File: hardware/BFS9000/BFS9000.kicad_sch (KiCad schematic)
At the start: 0 parts

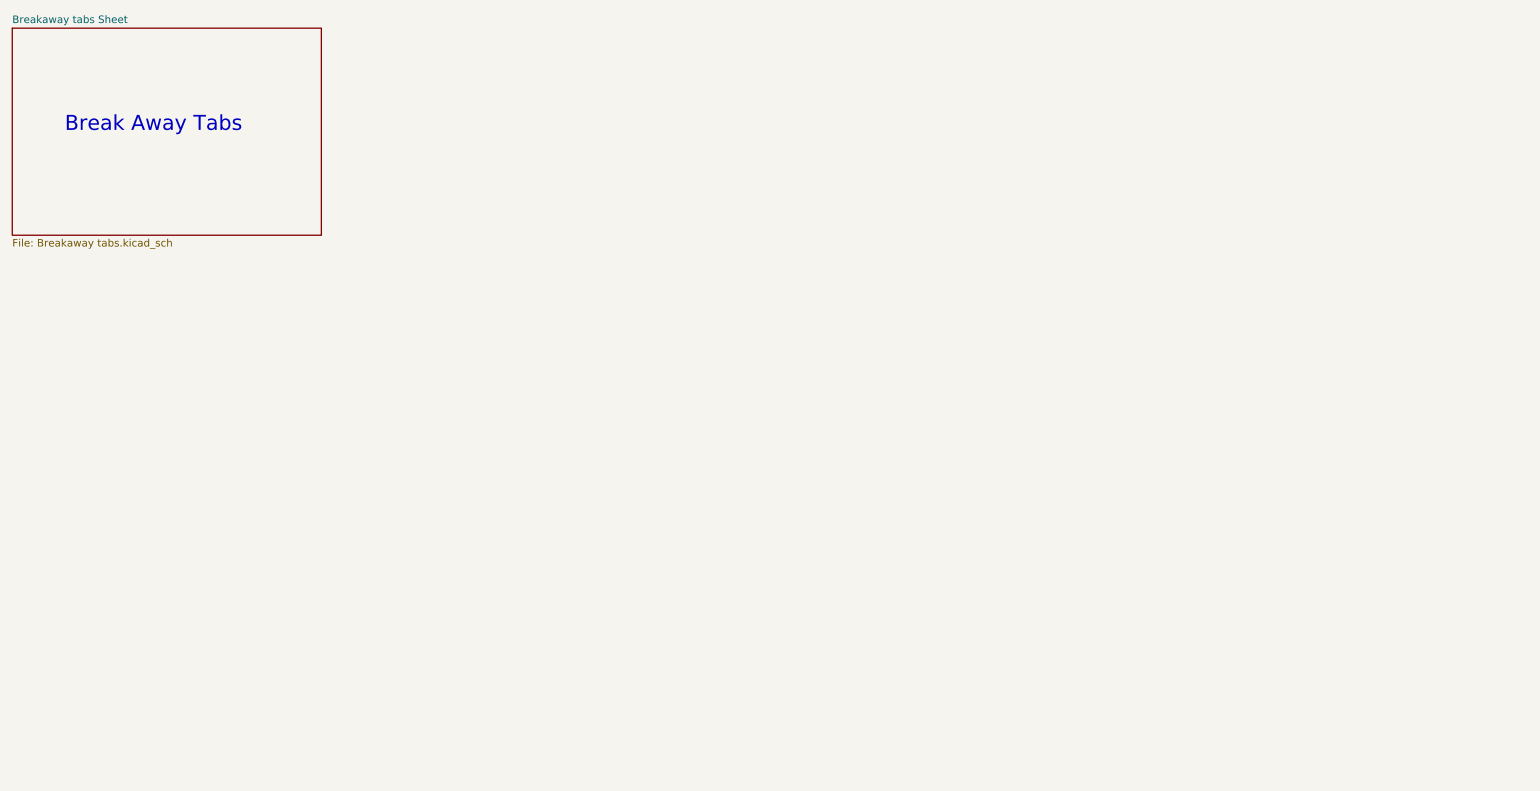
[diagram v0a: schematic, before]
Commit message: feat(hardware): add RP2040 footprint and peripheral circuitry
Add the RP2040 footprint, decoupling capacitors, OLED connectors, I2C pull-up resistors, and left/right keyboard side detection circuitry.
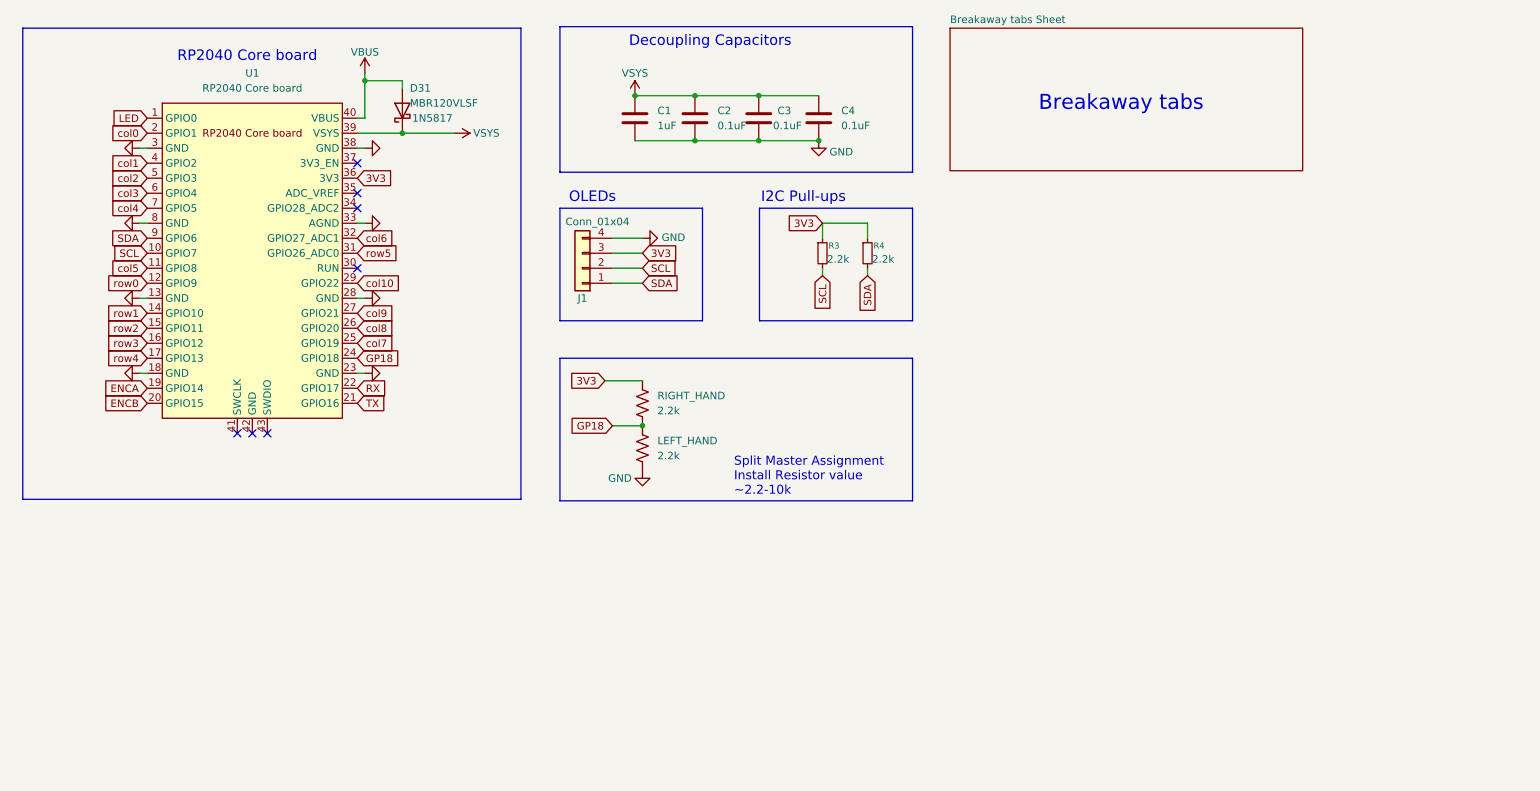
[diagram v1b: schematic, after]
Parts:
- added C1: 1uF, Capacitor_SMD:C_0805_2012Metric_Pad1.18x1.45mm_HandSolder, symbol Device:C
- added C2, C3, C4: 0.1uF, Capacitor_SMD:C_0805_2012Metric_Pad1.18x1.45mm_HandSolder, symbol Device:C
- added D31: MBR120VLSF, Sofle_Pico:D_SOD-123_DO-41_7.62mm_Hybrid_DoubleSided, symbol Diode:1N5817
- added J1: Conn_01x04, BFS9000:OLED SSD1306 128x64, symbol Connector_Generic:Conn_01x04
- added LEFT_HAND, RIGHT_HAND: 2.2k, BFS9000:Res_1206_SMD_6.3mm_TH_Hybrid, symbol Device:R_US
- added R3, R4: 2.2k, BFS9000:Res_1206_SMD_6.3mm_TH_Hybrid, symbol Device:R_Small
- added U1: RP2040 Core board, BFS9000:RPi_Pico_SMD_TH_DS, symbol BFS9000:Pico
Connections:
- new net 3V3: J1.3 (Pin_3), R3.1, R4.1, RIGHT_HAND.2, U1.36 (3V3)
- new net ENCA: U1.19 (GPIO14)
- new net ENCB: U1.20 (GPIO15)
- new net GND: C1.2, C2.2, C3.2, C4.2, J1.4 (Pin_4), LEFT_HAND.2, U1.13 (GND), U1.18 (GND), U1.23 (GND), U1.28 (GND), U1.3 (GND), U1.33 (AGND), U1.38 (GND), U1.8 (GND)
- new net GP18: LEFT_HAND.1, RIGHT_HAND.1, U1.24 (GPIO18)
- new net LED: U1.1 (GPIO0)
- new net RX: U1.22 (GPIO17)
- new net SCL: J1.2 (Pin_2), R3.2, U1.10 (GPIO7)
- new net SDA: J1.1 (Pin_1), R4.2, U1.9 (GPIO6)
- new net TX: U1.21 (GPIO16)
- new net VBUS: D31.2 (A), U1.40 (VBUS)
- new net VSYS: C1.1, C2.1, C3.1, C4.1, D31.1 (K), U1.39 (VSYS)
- new net col0: U1.2 (GPIO1)
- new net col1: U1.4 (GPIO2)
- new net col10: U1.29 (GPIO22)
- new net col2: U1.5 (GPIO3)
- new net col3: U1.6 (GPIO4)
- new net col4: U1.7 (GPIO5)
- new net col5: U1.11 (GPIO8)
- new net col6: U1.32 (GPIO27_ADC1)
- new net col7: U1.25 (GPIO19)
- new net col8: U1.26 (GPIO20)
- new net col9: U1.27 (GPIO21)
- new net row0: U1.12 (GPIO9)
- new net row1: U1.14 (GPIO10)
- new net row2: U1.15 (GPIO11)
- new net row3: U1.16 (GPIO12)
- new net row4: U1.17 (GPIO13)
- new net row5: U1.31 (GPIO26_ADC0)
- no-connect marks 0 -> 7
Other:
- note added: "Breakaway tabs"
- note added: "Decoupling Capacitors"
- note added: "I2C Pull-ups"
- note added: "OLEDs"
- note added: "RP2040 Core board"
- note added: "Split Master Assignment Install Resistor value ~2.2-10k"
- note removed: "Break Away Tabs"

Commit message: feat(hardware): integrate RGB and switch matrix layout
Add dedicated schematic sheets for addressable RGB LEDs and keyboard switches.

Place SK6803 MINI-E LEDs, MX switch footprints, stabilizers, rotary encoder, jack connector, and related power/control components in the BFS9000 PCB layout.

Update the main schematic, project settings, and breakaway tabs sheet to match the expanded hardware design.
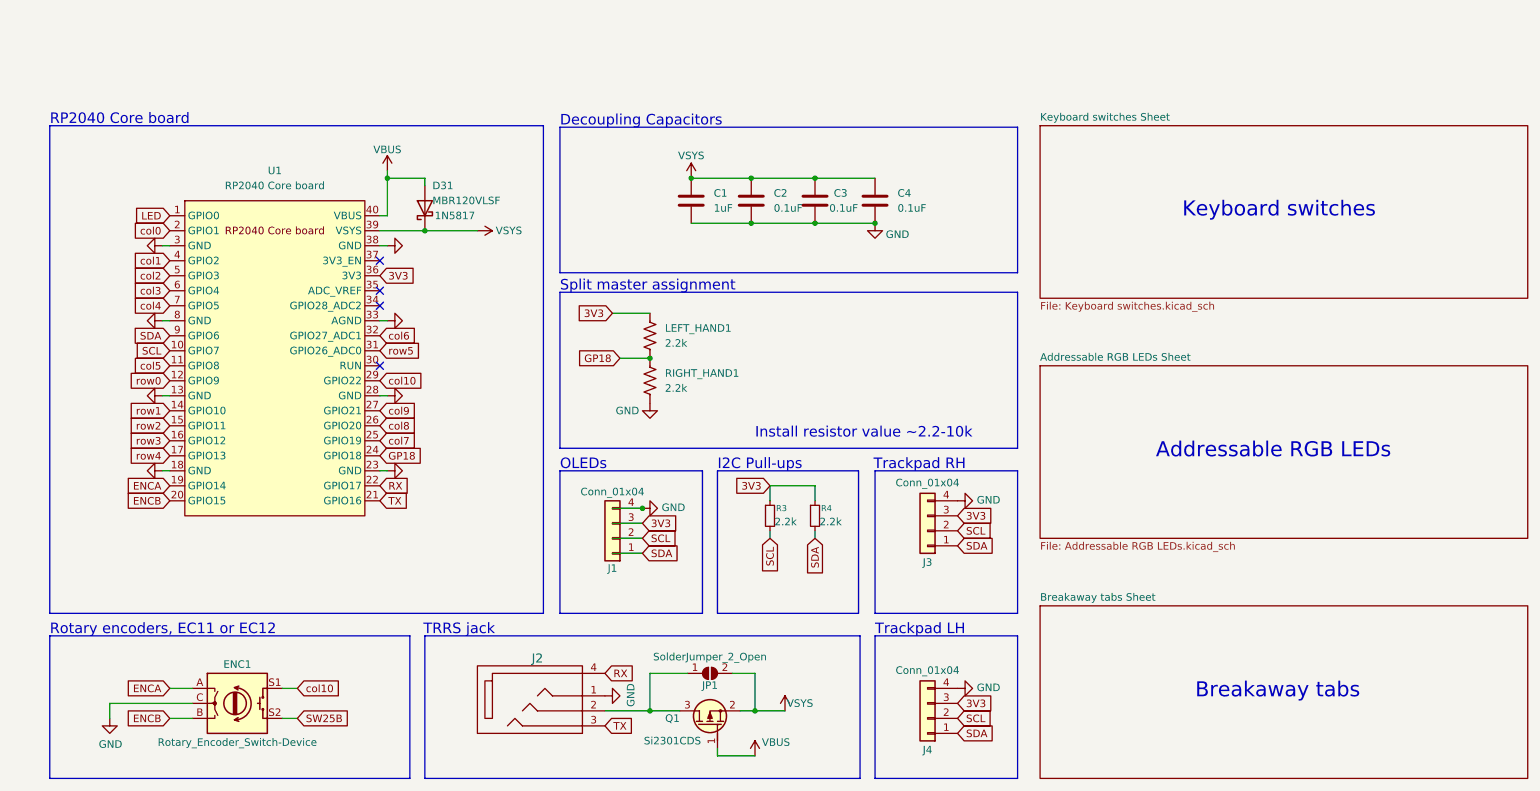
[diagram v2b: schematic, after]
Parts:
- added ENC1: Rotary_Encoder_Switch-Device, BFS9000:RotaryEncoder_Alps_EC11E-Switch_Vertical_H20mm-keebio_modified, symbol BFS9000:Rotary_Encoder_Switch-Device
- added J2: MJ-4PP-9, BFS9000:MJ-4PP-9, symbol BFS9000:MJ-4PP-9
- added J3, J4: Conn_01x04, BFS9000:Cirque tie in, symbol BFS9000:Conn_01x04
- added JP1: SolderJumper_2_Open, BFS9000:Level Shifter Bypass Jumper, symbol BFS9000:SolderJumper_2_Open
- added Q1: Si2301CDS, BFS9000:SOT-23_DS, symbol PCM_Transistor_MOSFET_AKL:DMG2305UX
- renumbered RIGHT_HAND to LEFT_HAND1, LEFT_HAND to RIGHT_HAND1
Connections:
- net 3V3: now also J3.3 (Pin_3), J4.3 (Pin_3)
- net ENCA: now also ENC1.A
- net ENCB: now also ENC1.B
- net GND: now also ENC1.C, J2.1, J3.4 (Pin_4), J4.4 (Pin_4)
- net RX: now also J2.4
- net SCL: now also J3.2 (Pin_2), J4.2 (Pin_2)
- net SDA: now also J3.1 (Pin_1), J4.1 (Pin_1)
- net TX: now also J2.3
- net VBUS: now also Q1.1 (G)
- net VSYS: now also JP1.2 (B), Q1.2 (S)
- net col10: now also ENC1.S1
- new net: J2.2, JP1.1 (A), Q1.3 (D)
- new net SW25B: ENC1.S2
- no-connect marks 7 -> 4
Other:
- added sheet Addressable RGB LEDs Sheet (Addressable RGB LEDs.kicad_sch)
- added sheet Keyboard switches Sheet (Keyboard switches.kicad_sch)
- note added: "Addressable RGB LEDs"
- note added: "Install resistor value ~2.2-10k"
- note added: "Keyboard switches"
- note added: "Rotary encoders, EC11 or EC12"
- note added: "Split master assignment"
- note added: "TRRS jack"
- note added: "Trackpad LH"
- note added: "Trackpad RH"
- note removed: "Split Master Assignment Install Resistor value ~2.2-10k"
- moved on the sheet: C1, C2, C3, C4, D31, J1, LEFT_HAND1, R3, R4, RIGHT_HAND1

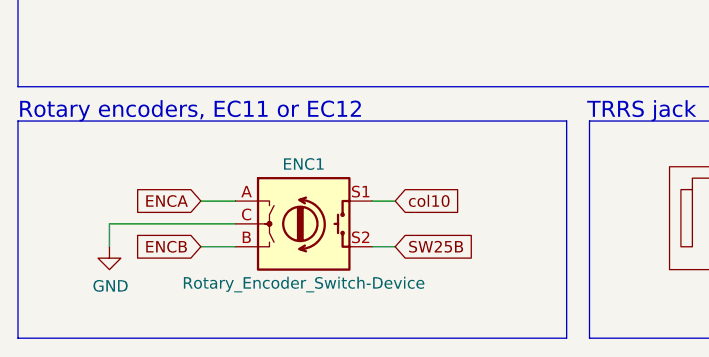
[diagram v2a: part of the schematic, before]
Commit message: feat(hardware): update BFS9000 schematic and PCB layout
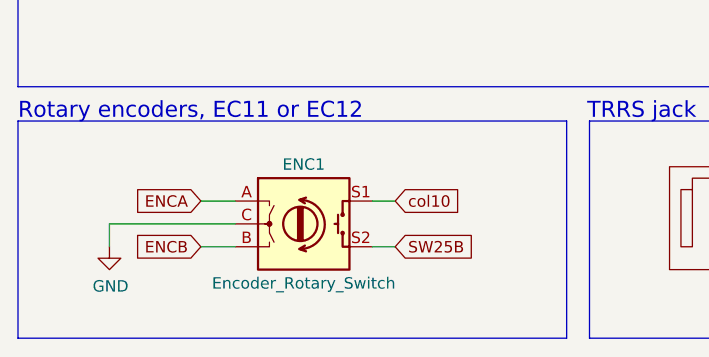
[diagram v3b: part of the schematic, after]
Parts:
- C1, C2, C3, C4: footprint Capacitor_SMD:C_0805_2012Metric_Pad1.18x1.45mm_HandSolder -> BFS9000:C_0805_HandSolder; symbol Device:C -> BFS9000:C
- D31: footprint Sofle_Pico:D_SOD-123_DO-41_7.62mm_Hybrid_DoubleSided -> BFS9000:D_Hybrid_SOD-123_DO-41_P7.62mm_DS; symbol Diode:1N5817 -> BFS9000:1N5817
- ENC1: value Rotary_Encoder_Switch-Device -> Encoder_Rotary_Switch; footprint BFS9000:RotaryEncoder_Alps_EC11E-Switch_Vertical_H20mm-keebio_modified -> BFS9000:Encoder_EC11E_Switch_Vertical_H20mm; symbol BFS9000:Rotary_Encoder_Switch-Device -> BFS9000:Encoder_Rotary_Switch
- J1: footprint BFS9000:OLED SSD1306 128x64 -> BFS9000:Display_OLED_SSD1306_128x64; symbol Connector_Generic:Conn_01x04 -> BFS9000:Conn_01x04
- J3, J4: footprint BFS9000:Cirque tie in -> BFS9000:Conn_Touchpad
- JP1: footprint BFS9000:Level Shifter Bypass Jumper -> BFS9000:SolderJumper_Level_Shifter_Bypass
- LEFT_HAND1, RIGHT_HAND1: footprint BFS9000:Res_1206_SMD_6.3mm_TH_Hybrid -> BFS9000:R_Hybrid_1206_P6.3mm; symbol Device:R_US -> BFS9000:R_US
- Q1: symbol PCM_Transistor_MOSFET_AKL:DMG2305UX -> BFS9000:DMG2305UX
- R3, R4: footprint BFS9000:Res_1206_SMD_6.3mm_TH_Hybrid -> BFS9000:R_Hybrid_1206_P6.3mm; symbol Device:R_Small -> BFS9000:R_Small
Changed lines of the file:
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@@
 	(generator "eeschema")
 	(generator_version "10.0")
-	(paper "A4")
+	(paper "A3")
 	(title_block
 		(title "BSF9000")
-		(date "2026-05-01")
-		(rev "0.3")
+		(date "2026-05-21")
+		(rev "0.4")
 		(company "jguillen-lab")
 		(comment 1 "Split ergonomic keyboard based on Sofle by Josef Adamčík")
@@
 	)
 	(symbol
-		(lib_id "power:VBUS")
+		(lib_id "BFS9000:VBUS")
 		(at 80.01 41.91 0)
 		(unit 1)
@@
 	)
 	(symbol
-		(lib_id "power:GND")
+		(lib_id "BFS9000:GND-power")
 		(at 162.56 50.8 0)
 		(unit 1)
@@
 	)
 	(symbol
-		(lib_id "Device:C")
+		(lib_id "BFS9000:C")
 		(at 141.605 46.99 0)
 		(unit 1)
@@
 			)
 		)
-		(property "Footprint" "Capacitor_SMD:C_0805_2012Metric_Pad1.18x1.45mm_HandSolder"
+		(property "Footprint" "BFS9000:C_0805_HandSolder"
 			(at 142.5702 50.8 0)
 			(hide yes)
@@
 	)
 	(symbol
-		(lib_id "power:GND")
+		(lib_id "BFS9000:GND-power")
 		(at 41.91 92.71 270)
 		(unit 1)
@@
 	(symbol
 		(lib_name "R_US_1")
-		(lib_id "Device:R_US")
+		(lib_id "BFS9000:R_US")
 		(at 124.46 77.47 0)
 		(unit 1)
@@
 			)
 		)
-		(property "Footprint" "BFS9000:Res_1206_SMD_6.3mm_TH_Hybrid"
+		(property "Footprint" "BFS9000:R_Hybrid_1206_P6.3mm"
 			(at 125.476 77.724 90)
 			(hide yes)
@@
 	)
 	(symbol
-		(lib_id "Device:C")
+		(lib_id "BFS9000:C")
 		(at 162.56 46.99 0)
 		(unit 1)
@@
 			)
 		)
-		(property "Footprint" "Capacitor_SMD:C_0805_2012Metric_Pad1.18x1.45mm_HandSolder"
+		(property "Footprint" "BFS9000:C_0805_HandSolder"
 			(at 163.5252 50.8 0)
 			(hide yes)
@@
 	)
 	(symbol
-		(lib_id "Connector_Generic:Conn_01x04")
+		(lib_id "BFS9000:Conn_01x04")
 		(at 118.11 104.14 180)
 		(unit 1)
@@
 			)
 		)
-		(property "Footprint" "BFS9000:OLED SSD1306 128x64"
+		(property "Footprint" "BFS9000:Display_OLED_SSD1306_128x64"
 			(at 118.11 104.14 0)
 			(hide yes)
@@
 	)
 	(symbol
-		(lib_id "power:GND")
+		(lib_id "BFS9000:GND-power")
 		(at 41.91 54.61 270)
 		(unit 1)
@@
 	)
 	(symbol
-		(lib_id "PCM_Transistor_MOSFET_AKL:DMG2305UX")
+		(lib_id "BFS9000:DMG2305UX")
 		(at 134.62 135.89 270)
 		(mirror x)
@@
 	)
 	(symbol
-		(lib_id "power:VDC")
+		(lib_id "BFS9000:VDC")
 		(at 131.445 43.18 0)
 		(unit 1)
@@
 	)
 	(symbol
-		(lib_id "power:GND")
+		(lib_id "BFS9000:GND-power")
 		(at 41.91 67.31 270)
 		(unit 1)
@@
 	)
 	(symbol
-		(lib_id "power:VDC")
+		(lib_id "BFS9000:VDC")
 		(at 95.25 52.07 270)
 		(unit 1)
@@
 			)
 		)
-		(property "Footprint" "BFS9000:Cirque tie in"
+		(property "Footprint" "BFS9000:Conn_Touchpad"
 			(at 171.45 134.62 0)
 			(hide yes)
@@
 	)
 	(symbol
-		(lib_id "Device:C")
+		(lib_id "BFS9000:C")
 		(at 152.4 46.99 0)
 		(unit 1)
@@
 			)
 		)
-		(property "Footprint" "Capacitor_SMD:C_0805_2012Metric_Pad1.18x1.45mm_HandSolder"
+		(property "Footprint" "BFS9000:C_0805_HandSolder"
 			(at 153.3652 50.8 0)
 			(hide yes)
@@
 	)
 	(symbol
-		(lib_id "power:VBUS")
+		(lib_id "BFS9000:VBUS")
 		(at 142.24 140.97 0)
 		(unit 1)
@@
 			)
 		)
-		(property "Footprint" "BFS9000:Level Shifter Bypass Jumper"
+		(property "Footprint" "BFS9000:SolderJumper_Level_Shifter_Bypass"
 			(at 134.62 127 0)
 			(hide yes)
@@
 	)
 	(symbol
-		(lib_id "Device:R_Small")
+		(lib_id "BFS9000:R_Small")
 		(at 144.78 100.33 0)
 		(unit 1)
@@
 			)
 		)
-		(property "Footprint" "BFS9000:Res_1206_SMD_6.3mm_TH_Hybrid"
+		(property "Footprint" "BFS9000:R_Hybrid_1206_P6.3mm"
 			(at 144.78 100.33 0)
 			(hide yes)
@@
 	)
 	(symbol
-		(lib_id "power:GND")
+		(lib_id "BFS9000:GND-power")
 		(at 80.01 92.71 90)
 		(unit 1)
@@
 	)
 	(symbol
-		(lib_id "BFS9000:Rotary_Encoder_Switch-Device")
+		(lib_id "BFS9000:Encoder_Rotary_Switch")
 		(at 54.61 132.08 0)
 		(unit 1)
@@
 			)
 		)
-		(property "Value" "Rotary_Encoder_Switch-Device"
+		(property "Value" "Encoder_Rotary_Switch"
 			(at 54.61 138.684 0)
 			(show_name no)
@@
 			)
 		)
-		(property "Footprint" "BFS9000:RotaryEncoder_Alps_EC11E-Switch_Vertical_H20mm-keebio_modified"
+		(property "Footprint" "BFS9000:Encoder_EC11E_Switch_Vertical_H20mm"
 			(at 50.8 128.016 0)
 			(hide yes)
@@
 	)
 	(symbol
-		(lib_id "power:GND")
+		(lib_id "BFS9000:GND-power")
 		(at 80.01 80.01 90)
 		(unit 1)
@@
 	)
 	(symbol
-		(lib_id "Diode:1N5817")
+		(lib_id "BFS9000:1N5817")
 		(at 86.36 48.26 90)
 		(unit 1)
@@
 			)
 		)
-		(property "Footprint" "Sofle_Pico:D_SOD-123_DO-41_7.62mm_Hybrid_DoubleSided"
+		(property "Footprint" "BFS9000:D_Hybrid_SOD-123_DO-41_P7.62mm_DS"
 			(at 90.805 48.26 0)
 			(hide yes)
@@
 	)
 	(symbol
-		(lib_id "Device:C")
+		(lib_id "BFS9000:C")
 		(at 131.445 46.99 0)
 		(unit 1)
@@
 			)
 		)
-		(property "Footprint" "Capacitor_SMD:C_0805_2012Metric_Pad1.18x1.45mm_HandSolder"
+		(property "Footprint" "BFS9000:C_0805_HandSolder"
 			(at 132.4102 50.8 0)
 			(hide yes)
@@
 	)
 	(symbol
-		(lib_id "power:GND")
+		(lib_id "BFS9000:GND-power")
 		(at 41.91 80.01 270)
 		(unit 1)
@@
 	)
 	(symbol
-		(lib_id "Device:R_Small")
+		(lib_id "BFS9000:R_Small")
 		(at 152.4 100.33 0)
 		(unit 1)
@@
 			)
 		)
-		(property "Footprint" "BFS9000:Res_1206_SMD_6.3mm_TH_Hybrid"
+		(property "Footprint" "BFS9000:R_Hybrid_1206_P6.3mm"
 			(at 152.4 100.33 0)
 			(hide yes)
@@
 	)
 	(symbol
-		(lib_id "power:GND")
+		(lib_id "BFS9000:GND-power")
 		(at 124.46 81.28 0)
 		(unit 1)
@@
 	)
 	(symbol
-		(lib_id "power:VDC")
+		(lib_id "BFS9000:VDC")
 		(at 147.32 133.35 0)
 		(unit 1)
@@
 	)
 	(symbol
-		(lib_id "power:GND")
+		(lib_id "BFS9000:GND-power")
 		(at 80.01 54.61 90)
 		(unit 1)
@@
 	)
 	(symbol
-		(lib_id "power:GND")
+		(lib_id "BFS9000:GND-power")
 		(at 80.01 67.31 90)
 		(unit 1)
@@
 			)
 		)
-		(property "Footprint" "BFS9000:Cirque tie in"
+		(property "Footprint" "BFS9000:Conn_Touchpad"
 			(at 171.45 102.87 0)
 			(hide yes)
@@
 	)
 	(symbol
-		(lib_id "Device:R_US")
+		(lib_id "BFS9000:R_US")
 		(at 124.46 69.85 180)
 		(unit 1)
@@
 			)
 		)
-		(property "Footprint" "BFS9000:Res_1206_SMD_6.3mm_TH_Hybrid"
+		(property "Footprint" "BFS9000:R_Hybrid_1206_P6.3mm"
 			(at 123.444 69.596 90)
 			(hide yes)
